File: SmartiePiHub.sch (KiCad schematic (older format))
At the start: 82 parts, among them P1 Conn_02x20_Odd_Even

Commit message: added rpi symbol
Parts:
- removed P1: Conn_02x20_Odd_Even, Connector_PinSocket_2.54mm:PinSocket_2x20_P2.54mm_Vertical, symbol Connector_Generic:Conn_02x20_Odd_Even
- added ?: RPI, symbol smartie-pi-raspi:RPI
- added SW?: SW_SPST, symbol Switch:SW_SPST
- added SW?: SW_Push, symbol Switch:SW_Push
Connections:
- net labels added: GPIO0(ID_SD), GPIO1(ID_SC), GPIO14(TXD), GPIO15(RXD), GPIO17, GPIO18(PCM_CLK), GPIO19(PCM_FS), GPIO20(PCM_DIN), GPIO21(PCM_DOUT), GPIO22, GPIO23, GPIO24, GPIO25, GPIO27, GPIO7(CE1), GPIO8(CE0)
- net labels removed: +3.3V, AIN1P, AIN2P, GPIO14(TXD0), GPIO15(RXD0), GPIO17(GEN0), GPIO18(GEN1)(PWM0), GPIO19(SPI1_MISO), GPIO20(SPI1_MOSI), GPIO21(SPI1_SCK), GPIO22(GEN3), GPIO23(GEN4), GPIO24(GEN5), GPIO25(GEN6), GPIO27(GEN2), GPIO7(SPI1_CE_N), GPIO8(SPI0_CE_N), ID_SC, ID_SD
- wire segments 401 -> 399
- no-connect marks 13 -> 15

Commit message: connected spi/i2s lines
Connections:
- net GPIO18(PCM_CLK) is gone; now on net I2S_CLK: ?.12 (GPIO18(PCM_CLK))
- net GPIO19(PCM_FS) is gone; now on net I2S_LRCLK: ?.35 (GPIO19(PCM_FS))
- net GPIO2(SDA1) is gone; now on net I2C_SDA: ?.3 (GPIO2(SDA))
- net GPIO20(PCM_DIN) is gone; now on net I2S_ADC: ?.38 (GPIO20(PCM_DIN))
- net GPIO21(PCM_DOUT) is gone; now on net I2S_DAC: ?.40 (GPIO21(PCM_DOUT))
- net GPIO3(SCL1) is gone; now on net I2C_SCL: ?.5 (GPIO3(SCL))
- net SPI1_MISO is gone; now on net SPI_MISO: CN?.3 (Pin_3), CN?.3 (Pin_3)
- net SPI1_MOSI is gone; now on net SPI_MOSI: CN?.2 (Pin_2), CN?.2 (Pin_2)
- net SPI1_SCK is gone; now on net SPI_SCLK: CN?.4 (Pin_4), CN?.4 (Pin_4)
- net SPI2_MISO is gone; now on net SPI_MISO: CN?.6 (Pin_6)
- net SPI2_MOSI is gone; now on net SPI_MOSI: CN?.3 (Pin_3)
- net SPI2_NSS_TRX is gone; now on net SPI_CE_SX1238: CN?.4 (Pin_4)
- net SPI2_SCK is gone; now on net SPI_SCLK: CN?.5 (Pin_5)
- net GPIO10(SPI0_MOSI) renamed SPI_MOSI
- net GPIO11(SPI0_SCK) renamed SPI_SCLK
- net GPIO14(TXD) renamed UART_TXD0
- net GPIO15(RXD) renamed UART_RXD0
- net GPIO7(CE1) renamed SPI_CE_SX1238
- net GPIO8(CE0) renamed SPI_CE0
- net GPIO9(SPI0_MISO) renamed SPI_MISO
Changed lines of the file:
@@
 	4350 2600 5400 2600
 Text Label 1300 1200 0    50   ~ 0
-GPIO2(SDA1)
+I2C_SDA
 Text Label 1300 1300 0    50   ~ 0
-GPIO3(SCL1)
+I2C_SCL
 Text Label 1300 1400 0    50   ~ 0
 GPIO4(GCLK)
@@
 GPIO22
 Text Label 1300 2000 0    50   ~ 0
-GPIO10(SPI0_MOSI)
+SPI_MOSI
 Text Label 1300 2100 0    50   ~ 0
-GPIO9(SPI0_MISO)
+SPI_MISO
 Text Label 1300 2200 0    50   ~ 0
-GPIO11(SPI0_SCK)
+SPI_SCLK
 Text Label 1300 2400 0    50   ~ 0
 GPIO0(ID_SD)
@@
 GPIO13(PWM1)
 Text Label 1300 2800 0    50   ~ 0
-GPIO19(PCM_FS)
+I2S_LRCLK
 Text Label 1300 2900 0    50   ~ 0
 GPIO26
 Text Label 5400 2900 2    50   ~ 0
-GPIO20(PCM_DIN)
+I2S_ADC
 Text Label 5400 2800 2    50   ~ 0
 GPIO16
@@
 GPIO1(ID_SC)
 Text Label 5400 2300 2    50   ~ 0
-GPIO7(CE1)
+SPI_CE_SX1238
 Text Label 5400 2200 2    50   ~ 0
-GPIO8(CE0)
+SPI_CE0
 Text Label 5400 2100 2    50   ~ 0
 GPIO25
@@
 GPIO23
 Text Label 5400 1600 2    50   ~ 0
-GPIO18(PCM_CLK)
+I2S_CLK
 Text Label 5400 1500 2    50   ~ 0
-GPIO15(RXD)
+UART_RXD0
 Text Label 5400 1400 2    50   ~ 0
-GPIO14(TXD)
+UART_TXD0
 Wire Wire Line
 	4450 1300 4350 1300
@@
 	4350 3000 5400 3000
 Text Label 5400 3000 2    50   ~ 0
-GPIO21(PCM_DOUT)
+I2S_DAC
 Wire Wire Line
 	4550 1100 4550 1200
@@
 	1    0    0    -1
 $EndComp
-Text Label 2700 4800 2    50   ~ 0
-SPI2_NSS_TRX
 Wire Wire Line
 	2700 4800 2150 4800
@@
 Wire Wire Line
 	2700 4700 2150 4700
-Text Label 2700 4900 2    50   ~ 0
-SPI2_MISO
 Wire Wire Line
 	2700 4900 2150 4900
@@
 Wire Wire Line
 	1650 4700 1100 4700
-Text Label 1100 4800 0    50   ~ 0
-SPI2_MOSI
 Wire Wire Line
 	1650 4800 1100 4800
@@
 	0    -1   -1   0
 $EndComp
-$Comp
-L power:GND #PWR?
-U 1 1 5EB51208
-P 1100 4700
-F 0 "#PWR?" H 1100 4450 50  0001 C CNN
-F 1 "GND" V 1105 4572 50  0000 R CNN
-F 2 "" H 1100 4700 50  0001 C CNN
-F 3 "" H 1100 4700 50  0001 C CNN
-	1    1100 4700
-	0    1    1    0
-$EndComp
-Text Label 1100 4900 0    50   ~ 0
-SPI2_SCK
 $Comp
 L power:GND #PWR?
@@
 Wire Wire Line
 	3850 6150 3450 6150
-Text Label 3450 6150 0    50   ~ 0
-SPI1_SCK
 Wire Wire Line
 	3850 6050 3450 6050
-Text Label 3450 6050 0    50   ~ 0
-SPI1_MISO
 Wire Wire Line
 	3850 5950 3450 5950
-Text Label 3450 5950 0    50   ~ 0
-SPI1_MOSI
 Wire Wire Line
 	3850 5850 3450 5850
@@
 Wire Wire Line
 	3850 5200 3450 5200
-Text Label 3450 5200 0    50   ~ 0
-SPI1_SCK
 Wire Wire Line
 	3850 5100 3450 5100
-Text Label 3450 5100 0    50   ~ 0
-SPI1_MISO
 Wire Wire Line
 	3850 5000 3450 5000
-Text Label 3450 5000 0    50   ~ 0
-SPI1_MOSI
 Wire Wire Line
 	3850 4900 3450 4900
@@
 	1    0    0    -1
 $EndComp
+Text Label 2700 4800 2    50   ~ 0
+SPI_CE_SX1238
+$Comp
+L power:GND #PWR?
+U 1 1 5EB51208
+P 1100 4700
+F 0 "#PWR?" H 1100 4450 50  0001 C CNN
+F 1 "GND" V 1105 4572 50  0000 R CNN
+F 2 "" H 1100 4700 50  0001 C CNN
+F 3 "" H 1100 4700 50  0001 C CNN
+	1    1100 4700
+	0    1    1    0
+$EndComp
+Text Label 1100 4800 0    50   ~ 0
+SPI_MOSI
+Text Label 1100 4900 0    50   ~ 0
+SPI_SCLK
+Text Label 2700 4900 2    50   ~ 0
+SPI_MISO
+Text Label 3450 5100 0    50   ~ 0
+SPI_MISO
+Text Label 3450 5000 0    50   ~ 0
+SPI_MOSI
+Text Label 3450 5200 0    50   ~ 0
+SPI_SCLK
+Text Label 3450 5950 0    50   ~ 0
+SPI_MOSI
+Text Label 3450 6050 0    50   ~ 0
+SPI_MISO
+Text Label 3450 6150 0    50   ~ 0
+SPI_SCLK
 $EndSCHEMATC

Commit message: hooking up i2c bus
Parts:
- added R? (x2): 10K, symbol Device:R_Small
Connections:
- net SCL is gone; now on net I2C_SCL: U?.5 (SCL)
- net SDA is gone; now on net I2C_SDA: U?.6 (SDA)
- net +3V3: now also R?.1, R?.1
- net GND: now also BT?.2 (-), C?.2, R?.1, R?.1, R?.2
- net I2C_SCL: now also R?.2
- net I2C_SDA: now also R?.2
- net MICBIAS: no longer names the net of C?.2, C?.2, U?.1 (MICBIAS)
- net SPI_CE0 renamed SPI_CE_ZWAVE
- net SPI_CE_ZWAVE: now also CN?.1 (Pin_1)
- net ZWAVE_CS renamed SPI_CE_ZIGBEE
- net SPI_CE_ZIGBEE: no longer CN?.1 (Pin_1)
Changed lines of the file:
@@
 SPI_CE_SX1238
 Text Label 5400 2200 2    50   ~ 0
-SPI_CE0
+SPI_CE_ZWAVE
 Text Label 5400 2100 2    50   ~ 0
 GPIO25
@@
 Wire Wire Line
 	7300 2250 6950 2250
-Text Label 6200 2250 0    50   ~ 0
-MICBIAS
 $Comp
 L Device:C_Small C?
@@
 Wire Wire Line
 	6600 2050 6600 2250
-Connection ~ 6600 2250
-Wire Wire Line
-	6600 2250 6200 2250
 $Comp
 L Device:C_Small C?
@@
 	13200 1650 13200 1250
 Wire Wire Line
-	13200 1250 12550 1250
+	13200 1250 13050 1250
 Connection ~ 12550 1250
 Text Label 11600 1250 0    50   ~ 0
 +3V3
-Wire Wire Line
-	13350 1800 13100 1800
-Wire Wire Line
-	13350 1900 13100 1900
-Text Label 13100 1800 0    50   ~ 0
-SCL
-Text Label 13100 1900 0    50   ~ 0
-SDA
 $Comp
 L Device:R R?
@@
 Wire Wire Line
 	3850 5850 3450 5850
-Text Label 3450 5850 0    50   ~ 0
-ZWAVE_CS
 Wire Wire Line
 	4750 6350 4350 6350
@@
 	3850 4900 3450 4900
 Text Label 3450 4900 0    50   ~ 0
-ZWAVE_CS
+SPI_CE_ZIGBEE
 Wire Wire Line
 	4750 5400 4350 5400
@@
 Text Label 3450 6150 0    50   ~ 0
 SPI_SCLK
+Text Label 3450 5850 0    50   ~ 0
+SPI_CE_ZWAVE
+$Comp
+L Device:R_Small R?
+U 1 1 5F70A49C
+P 13050 1500
+F 0 "R?" H 13100 1600 50  0000 L CNN
+F 1 "10K" H 13100 1400 50  0000 L CNN
+F 2 "" H 13050 1500 50  0001 C CNN
+F 3 "~" H 13050 1500 50  0001 C CNN
+	1    13050 1500
+	1    0    0    -1
+$EndComp
+$Comp
+L Device:R_Small R?
+U 1 1 5F709D2C
+P 12850 1500
+F 0 "R?" H 12900 1600 50  0000 L CNN
+F 1 "10K" H 12900 1400 50  0000 L CNN
+F 2 "" H 12850 1500 50  0001 C CNN
+F 3 "~" H 12850 1500 50  0001 C CNN
+	1    12850 1500
+	1    0    0    -1
+$EndComp
+Wire Wire Line
+	12650 1900 12850 1900
+Wire Wire Line
+	12650 1800 13050 1800
+Wire Wire Line
+	13050 1600 13050 1800
+Connection ~ 13050 1800
+Wire Wire Line
+	13050 1800 13350 1800
+Wire Wire Line
+	12850 1600 12850 1900
+Connection ~ 12850 1900
+Wire Wire Line
+	12850 1900 13350 1900
+Wire Wire Line
+	12850 1400 12850 1250
+Connection ~ 12850 1250
+Wire Wire Line
+	12850 1250 12550 1250
+Wire Wire Line
+	13050 1400 13050 1250
+Connection ~ 13050 1250
+Wire Wire Line
+	13050 1250 12850 1250
+Text Label 12650 1900 0    50   ~ 0
+I2C_SDA
+Text Label 12650 1800 0    50   ~ 0
+I2C_SCL
+$Comp
+L power:GND #PWR?
+U 1 1 5F861A89
+P 13050 5500
+F 0 "#PWR?" H 13050 5250 50  0001 C CNN
+F 1 "GND" H 13055 5327 50  0000 C CNN
+F 2 "" H 13050 5500 50  0001 C CNN
+F 3 "" H 13050 5500 50  0001 C CNN
+	1    13050 5500
+	1    0    0    -1
+$EndComp
+Wire Wire Line
+	13050 5500 13050 5250
+$Comp
+L power:GND #PWR?
+U 1 1 5F88D6A0
+P 13300 5500
+F 0 "#PWR?" H 13300 5250 50  0001 C CNN
+F 1 "GND" H 13305 5327 50  0000 C CNN
+F 2 "" H 13300 5500 50  0001 C CNN
+F 3 "" H 13300 5500 50  0001 C CNN
+	1    13300 5500
+	1    0    0    -1
+$EndComp
+$Comp
+L power:GND #PWR?
+U 1 1 5F88DA3C
+P 13850 5500
+F 0 "#PWR?" H 13850 5250 50  0001 C CNN
+F 1 "GND" H 13855 5327 50  0000 C CNN
+F 2 "" H 13850 5500 50  0001 C CNN
+F 3 "" H 13850 5500 50  0001 C CNN
+	1    13850 5500
+	1    0    0    -1
+$EndComp
+$Comp
+L power:GND #PWR?
+U 1 1 5F88DD72
+P 14150 5500
+F 0 "#PWR?" H 14150 5250 50  0001 C CNN
+F 1 "GND" H 14155 5327 50  0000 C CNN
+F 2 "" H 14150 5500 50  0001 C CNN
+F 3 "" H 14150 5500 50  0001 C CNN
+	1    14150 5500
+	1    0    0    -1
+$EndComp
+$Comp
+L power:GND #PWR?
+U 1 1 5F88DF79
+P 14650 5500
+F 0 "#PWR?" H 14650 5250 50  0001 C CNN
+F 1 "GND" H 14655 5327 50  0000 C CNN
+F 2 "" H 14650 5500 50  0001 C CNN
+F 3 "" H 14650 5500 50  0001 C CNN
+	1    14650 5500
+	1    0    0    -1
+$EndComp
+Wire Wire Line
+	14650 5500 14650 5000
+Wire Wire Line
+	14150 5500 14150 5300
+Wire Wire Line
+	13850 5500 13850 5300
+Wire Wire Line
+	13300 5500 13300 5300
 $EndSCHEMATC

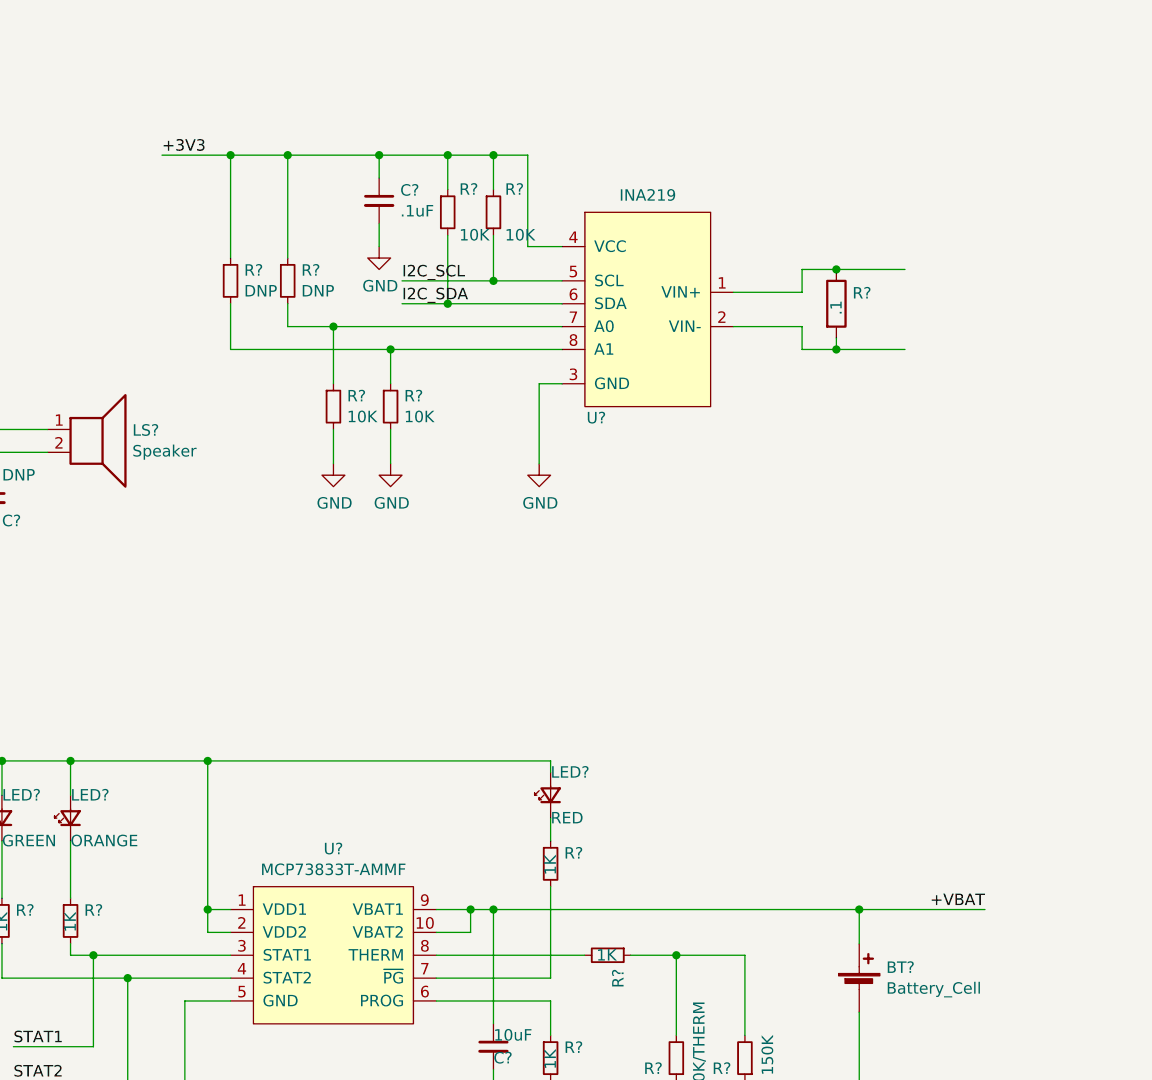
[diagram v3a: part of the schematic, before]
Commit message: added endpoints for ina219 shunt resistor and battery load
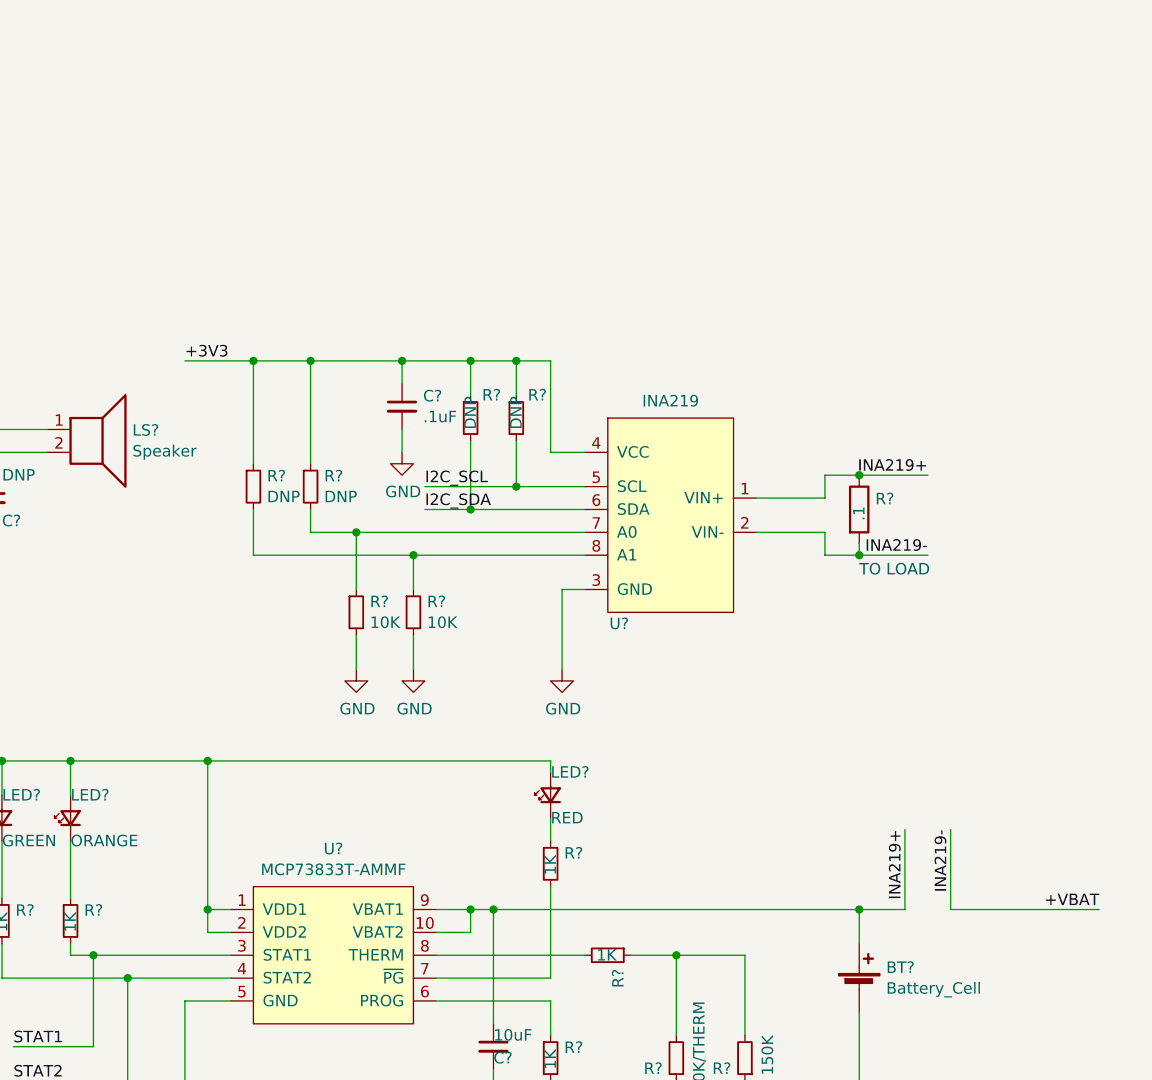
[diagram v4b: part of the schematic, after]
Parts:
- R? (x2): value 10K -> DNP
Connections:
- net +VBAT: now also R?.2, U?.2 (VIN-); no longer BT?.1 (+), C?.1, U?.10 (VBAT2), U?.9 (VBAT1)
- net INA219+: now reaches R?.1, U?.1 (VIN+)
- net INA219+: now also BT?.1 (+), C?.1, U?.10 (VBAT2), U?.9 (VBAT1)
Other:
- note added: "TO LOAD"
- moved on the sheet: C?, R?, U?

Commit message: cleaning up GPIO labels. routing power switch, buttons.
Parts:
- added C? (x2): 4.7uF, symbol Device:C_Small
- added R? (x2): 10K, symbol Device:R_Small
- added SW?: SW_Push, symbol Switch:SW_Push
- LED?: value ORANGE -> DNP
- LED?: value GREEN -> DNP
- R? (x2): value 1K -> DNP
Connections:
- net +3V3: now also R?.2, R?.2
- net +VBAT: now also SW?.2 (B); no longer R?.2, U?.2 (VIN-)
- net GND: now also SW?.2, SW?.2
- net INA219-: now reaches SW?.1 (A)
- net INA219-: now also R?.2, U?.2 (VIN-)
- net at SW?.1: now also R?.1
- net GPIO0(ID_SD): no longer names the net of ?.27 (GPIO0(ID_SD))
- net GPIO1(ID_SC): no longer names the net of ?.28 (GPIO1(ID_SC))
- net GPIO12(PWM0) renamed NEOPIXEL_DIN
- net GPIO13(PWM1): no longer names the net of ?.33 (GPIO13(PWM1))
- net GPIO16: no longer names the net of ?.36 (GPIO16)
- net GPIO17: no longer names the net of ?.11 (GPIO17)
- net GPIO22: no longer names the net of ?.15 (GPIO22)
- net GPIO23: no longer names the net of ?.16 (GPIO23)
- net GPIO24: no longer names the net of ?.18 (GPIO24)
- net GPIO25: no longer names the net of ?.22 (GPIO25)
- net GPIO26: no longer names the net of ?.37 (GPIO26)
- net GPIO27: no longer names the net of ?.13 (GPIO27)
- net GPIO4(GCLK): no longer names the net of ?.7 (GPIO4(GPCLK0))
- net GPIO5: no longer names the net of ?.29 (GPIO5)
- net GPIO6: no longer names the net of ?.31 (GPIO6)
- net UART_RXD0: no longer names the net of ?.10 (GPIO15(RXD))
- net UART_TXD0: no longer names the net of ?.8 (GPIO14(TXD))
- new net: R?.1, SW?.1
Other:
- moved on the sheet: SW?
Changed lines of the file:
@@
 	1300 1300 2450 1300
 Wire Wire Line
-	1300 1400 2450 1400
-Wire Wire Line
-	2450 1600 1300 1600
-Wire Wire Line
-	1300 1700 2450 1700
-Wire Wire Line
-	1300 1800 2450 1800
-Wire Wire Line
 	2450 2000 1300 2000
 Wire Wire Line
@@
 	1300 2200 2450 2200
 Wire Wire Line
-	2450 2400 1300 2400
-Wire Wire Line
-	1300 2500 2450 2500
-Wire Wire Line
-	1300 2600 2450 2600
-Wire Wire Line
-	2450 2700 1300 2700
-Wire Wire Line
 	1300 2800 2450 2800
 Wire Wire Line
-	1300 2900 2450 2900
-Wire Wire Line
-	4350 2800 5400 2800
-Wire Wire Line
 	4350 2900 5400 2900
 Wire Wire Line
 	4350 2300 5400 2300
 Wire Wire Line
-	4350 2400 5400 2400
-Wire Wire Line
-	4350 2100 5400 2100
-Wire Wire Line
 	4350 2200 5400 2200
 Wire Wire Line
-	4350 1800 5400 1800
-Wire Wire Line
-	4350 1900 5400 1900
-Wire Wire Line
-	4350 1500 5400 1500
-Wire Wire Line
 	4350 1600 5400 1600
-Wire Wire Line
-	4350 1400 5400 1400
-Wire Wire Line
-	4350 2600 5400 2600
 Text Label 1300 1200 0    50   ~ 0
 I2C_SDA
 Text Label 1300 1300 0    50   ~ 0
 I2C_SCL
-Text Label 1300 1400 0    50   ~ 0
-GPIO4(GCLK)
-Text Label 1300 1600 0    50   ~ 0
-GPIO17
-Text Label 1300 1700 0    50   ~ 0
-GPIO27
-Text Label 1300 1800 0    50   ~ 0
-GPIO22
 Text Label 1300 2000 0    50   ~ 0
 SPI_MOSI
@@
 Text Label 1300 2200 0    50   ~ 0
 SPI_SCLK
-Text Label 1300 2400 0    50   ~ 0
-GPIO0(ID_SD)
-Text Label 1300 2500 0    50   ~ 0
-GPIO5
-Text Label 1300 2600 0    50   ~ 0
-GPIO6
-Text Label 1300 2700 0    50   ~ 0
-GPIO13(PWM1)
 Text Label 1300 2800 0    50   ~ 0
 I2S_LRCLK
-Text Label 1300 2900 0    50   ~ 0
-GPIO26
 Text Label 5400 2900 2    50   ~ 0
 I2S_ADC
-Text Label 5400 2800 2    50   ~ 0
-GPIO16
-Text Label 5400 2600 2    50   ~ 0
-GPIO12(PWM0)
-Text Label 5400 2400 2    50   ~ 0
-GPIO1(ID_SC)
 Text Label 5400 2300 2    50   ~ 0
 SPI_CE_SX1238
 Text Label 5400 2200 2    50   ~ 0
 SPI_CE_ZWAVE
-Text Label 5400 2100 2    50   ~ 0
-GPIO25
-Text Label 5400 1900 2    50   ~ 0
-GPIO24
-Text Label 5400 1800 2    50   ~ 0
-GPIO23
 Text Label 5400 1600 2    50   ~ 0
 I2S_CLK
-Text Label 5400 1500 2    50   ~ 0
-UART_RXD0
-Text Label 5400 1400 2    50   ~ 0
-UART_TXD0
 Wire Wire Line
 	4450 1300 4350 1300
@@
 P 11200 4600
 F 0 "R?" H 11259 4646 50  0000 L CNN
-F 1 "1K" V 11200 4550 50  0000 L CNN
+F 1 "DNP" V 11200 4550 50  0000 L CNN
 F 2 "" H 11200 4600 50  0001 C CNN
 F 3 "~" H 11200 4600 50  0001 C CNN
@@
 P 10900 4600
 F 0 "R?" H 10959 4646 50  0000 L CNN
-F 1 "1K" V 10900 4550 50  0000 L CNN
+F 1 "DNP" V 10900 4550 50  0000 L CNN
 F 2 "" H 10900 4600 50  0001 C CNN
 F 3 "~" H 10900 4600 50  0001 C CNN
@@
 P 11200 4150
 F 0 "LED?" V 11300 4150 50  0000 R CNN
-F 1 "ORANGE" V 11100 4150 50  0000 R CNN
+F 1 "DNP" V 11100 4150 50  0000 R CNN
 F 2 "" V 11200 4150 50  0001 C CNN
 F 3 "~" V 11200 4150 50  0001 C CNN
@@
 P 10900 4150
 F 0 "LED?" V 11000 4150 50  0000 R CNN
-F 1 "GREEN" V 10800 4150 50  0000 R CNN
+F 1 "DNP" V 10800 4150 50  0000 R CNN
 F 2 "" V 10900 4150 50  0001 C CNN
 F 3 "~" V 10900 4150 50  0001 C CNN
@@
 Wire Wire Line
 	13050 4550 14650 4550
-Text Label 15700 4550 2    50   ~ 0
+Text Label 15950 4550 2    50   ~ 0
 +VBAT
 $Comp
@@
 L Switch:SW_SPST SW?
 U 1 1 5EE937D6
-P 10400 8450
-F 0 "SW?" H 10400 8685 50  0000 C CNN
-F 1 "SW_SPST" H 10400 8594 50  0000 C CNN
-F 2 "" H 10400 8450 50  0001 C CNN
-F 3 "~" H 10400 8450 50  0001 C CNN
-	1    10400 8450
+P 15450 4550
+F 0 "SW?" H 15450 4785 50  0000 C CNN
+F 1 "SW_SPST" H 15450 4694 50  0000 C CNN
+F 2 "" H 15450 4550 50  0001 C CNN
+F 3 "~" H 15450 4550 50  0001 C CNN
+	1    15450 4550
 	1    0    0    -1
 $EndComp
@@
 Connection ~ 14650 4550
 Wire Wire Line
-	15050 4550 15700 4550
-Wire Wire Line
 	14650 2650 14950 2650
 Connection ~ 14650 2650
@@
 Text Notes 14650 3100 0    50   ~ 0
 TO LOAD
+$Comp
+L Device:C_Small C?
+U 1 1 5FC8A77E
+P 13350 6700
+F 0 "C?" H 13350 6750 50  0000 L CNN
+F 1 "4.7uF" H 13350 6600 50  0000 L CNN
+F 2 "" H 13350 6700 50  0001 C CNN
+F 3 "~" H 13350 6700 50  0001 C CNN
+	1    13350 6700
+	1    0    0    -1
+$EndComp
+$Comp
+L Device:C_Small C?
+U 1 1 5FC8B279
+P 15350 4900
+F 0 "C?" H 15350 4950 50  0000 L CNN
+F 1 "4.7uF" H 15350 4800 50  0000 L CNN
+F 2 "" H 15350 4900 50  0001 C CNN
+F 3 "~" H 15350 4900 50  0001 C CNN
+	1    15350 4900
+	1    0    0    -1
+$EndComp
+$Comp
+L Device:R_Small R?
+U 1 1 5FE2E247
+P 11000 8700
+F 0 "R?" V 11100 8650 50  0000 L CNN
+F 1 "10K" V 11000 8650 50  0000 L CNN
+F 2 "" H 11000 8700 50  0001 C CNN
+F 3 "~" H 11000 8700 50  0001 C CNN
+	1    11000 8700
+	1    0    0    -1
+$EndComp
+Wire Wire Line
+	11500 8450 11600 8450
+$Comp
+L power:GND #PWR?
+U 1 1 5FE596AB
+P 11600 8450
+F 0 "#PWR?" H 11600 8200 50  0001 C CNN
+F 1 "GND" V 11605 8322 50  0000 R CNN
+F 2 "" H 11600 8450 50  0001 C CNN
+F 3 "" H 11600 8450 50  0001 C CNN
+	1    11600 8450
+	0    -1   -1   0
+$EndComp
+Wire Wire Line
+	11100 8450 11000 8450
+Wire Wire Line
+	11000 8450 11000 8600
+Wire Wire Line
+	11000 8450 10600 8450
+Connection ~ 11000 8450
+Wire Wire Line
+	11000 8800 11000 9050
+Text Label 11000 9050 1    50   ~ 0
++3V3
+Wire Wire Line
+	15250 4550 15050 4550
+Wire Wire Line
+	15650 4550 15950 4550
+$Comp
+L Switch:SW_Push SW?
+U 1 1 5FFFC823
+P 11300 9300
+F 0 "SW?" H 11300 9585 50  0000 C CNN
+F 1 "SW_Push" H 11300 9494 50  0000 C CNN
+F 2 "" H 11300 9500 50  0001 C CNN
+F 3 "~" H 11300 9500 50  0001 C CNN
+	1    11300 9300
+	1    0    0    -1
+$EndComp
+$Comp
+L Device:R_Small R?
+U 1 1 5FFFC829
+P 11000 9550
+F 0 "R?" V 11100 9500 50  0000 L CNN
+F 1 "10K" V 11000 9500 50  0000 L CNN
+F 2 "" H 11000 9550 50  0001 C CNN
+F 3 "~" H 11000 9550 50  0001 C CNN
+	1    11000 9550
+	1    0    0    -1
+$EndComp
+Wire Wire Line
+	11500 9300 11600 9300
+$Comp
+L power:GND #PWR?
+U 1 1 5FFFC830
+P 11600 9300
+F 0 "#PWR?" H 11600 9050 50  0001 C CNN
+F 1 "GND" V 11605 9172 50  0000 R CNN
+F 2 "" H 11600 9300 50  0001 C CNN
+F 3 "" H 11600 9300 50  0001 C CNN
+	1    11600 9300
+	0    -1   -1   0
+$EndComp
+Wire Wire Line
+	11100 9300 11000 9300
+Wire Wire Line
+	11000 9300 11000 9450
+Wire Wire Line
+	11000 9300 10600 9300
+Connection ~ 11000 9300
+Wire Wire Line
+	11000 9650 11000 9900
+Text Label 11000 9900 1    50   ~ 0
++3V3
+Text Label 5400 2600 2    50   ~ 0
+NEOPIXEL_DIN
+Wire Wire Line
+	4350 2600 5400 2600
 $EndSCHEMATC
